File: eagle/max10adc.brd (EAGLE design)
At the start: 98 x 62 mm, 189 parts, among them IC1 MAX19506, IC2 MAX19506, J1 MOLEX_BNC_73100-0105, J2 MOLEX_BNC_73100-0105, J3 MOLEX_BNC_73100-0105, J4 MOLEX_BNC_73100-0105, K1 AQY21SOP, K2 AQY21SOP, K3 AQY21SOP, K4 AQY21SOP, K5 AQY21SOP, K6 AQY21SOP, K7 AQY21SOP, K8 AQY21SOP, U1 MAX4416ESA, U2 MAX4416ESA, U340G CH340G, Y1 ABL-12.000MHZ-B2

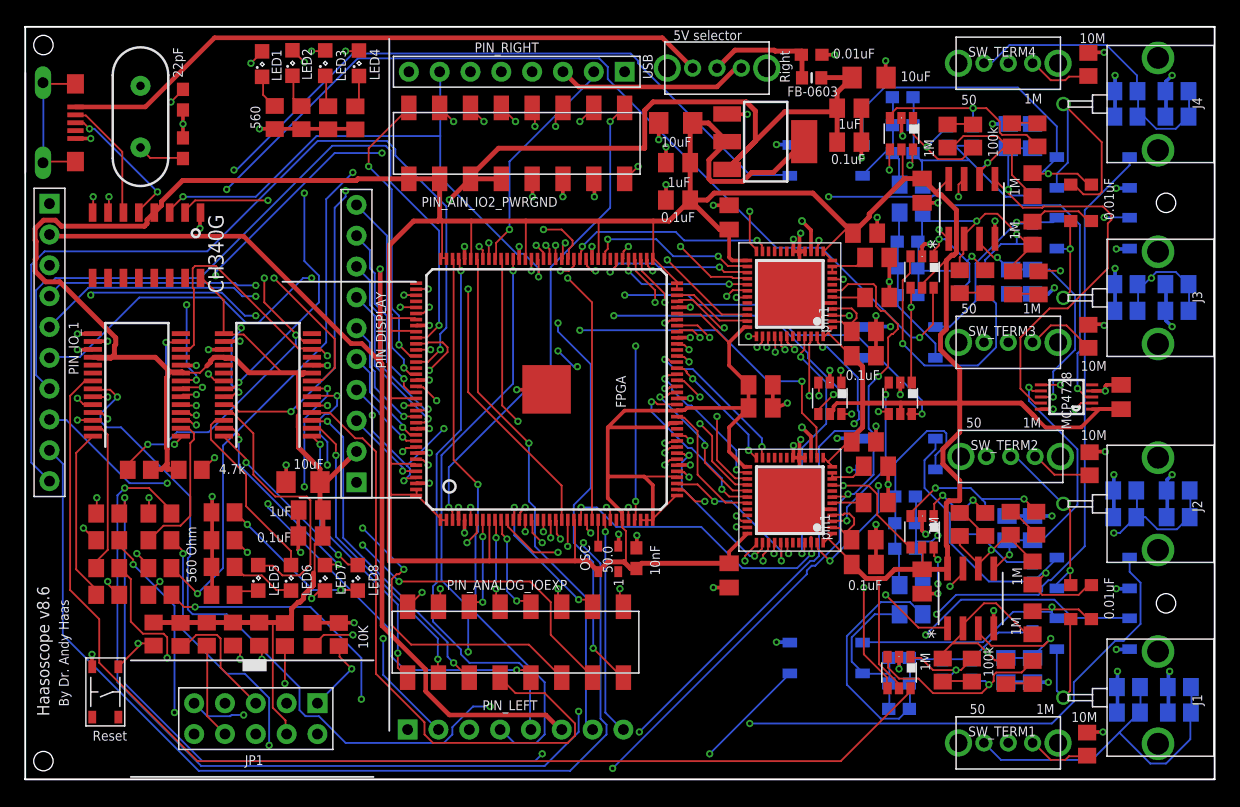
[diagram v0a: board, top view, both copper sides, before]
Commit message: for 8.7 with separate VCCA
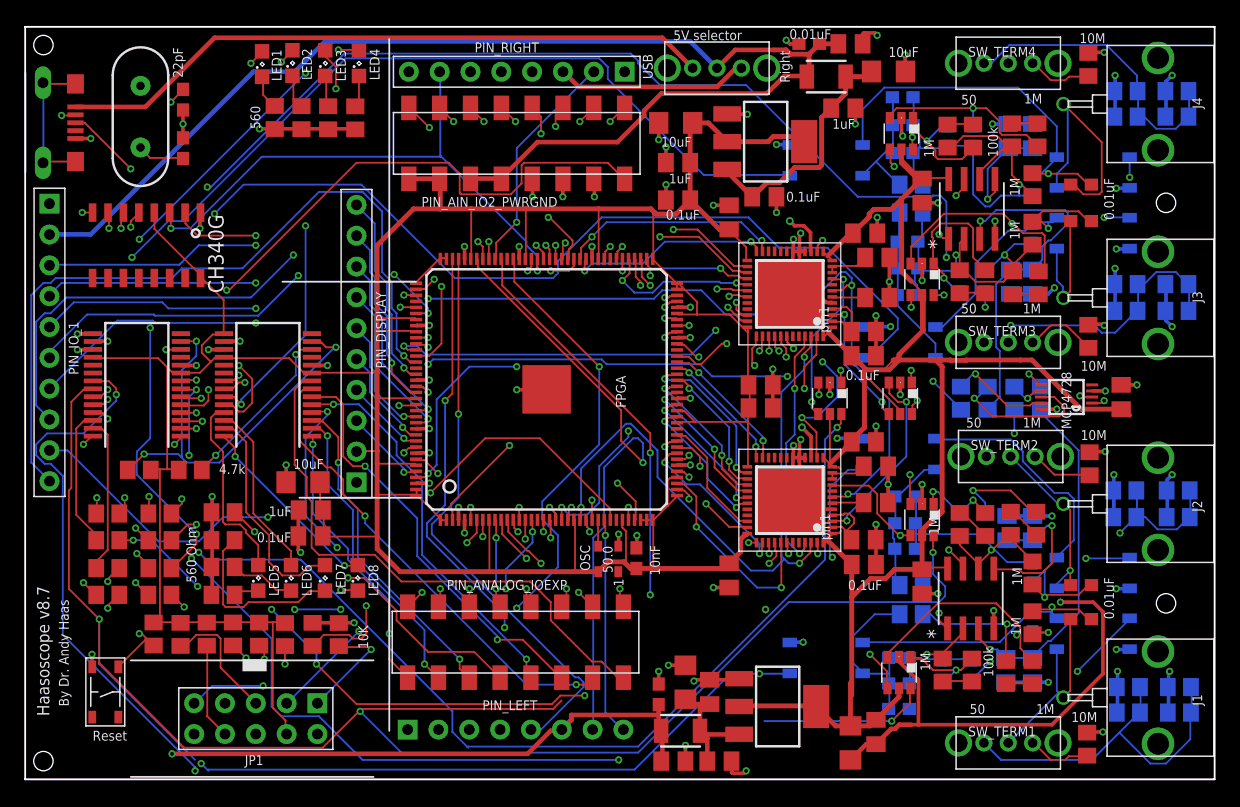
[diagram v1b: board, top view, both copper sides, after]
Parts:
- removed 5VBEAD: FB-0603, rcl:L0603
- added CP10, CP11, CP7, CP9: 1uF, rcl:C0805K
- added CP3, CP4: 10uF, rcl@1:C1206
- added CP8: 0.1uF, rcl:C0805K
- added C_5V_10NF1: 0.01uF, rcl@1:C0603
- added L1, L2: 10uH, SparkFun-Passives:1210
- added REG1: LDL1117S33R, Seeed-IC-2016:SOT-223
- added ROFFSET1, ROFFSET2, ROFFSET3, ROFFSET4: 200, rcl@1:R0805
- COFFSETB11, COFFSETB5, COFFSETB7, COFFSETB9: value 1uF -> 10uF
- moved CP2 8.32 mm to (48.9, 46.0)
- moved CP5 1.68 mm to (59.1, 56.3)
- moved GAINSW2 1.00 mm to (61.9, 19.4)
- moved C_5V_10NF 0.92 mm to (52.6, 58.6)
- moved GAINSW3 0.60 mm to (61.9, 39.2)
- moved CP1 0.50 mm to (55.4, 53.3)
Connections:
- removed net 5V_IN: 5VBEAD.2, C_5V_10NF.1, SW_5V.2
- new net N$44: DAC1.6, ROFFSET1.2
- new net N$45: DAC1.7, ROFFSET2.2
- new net N$46: DAC1.8, ROFFSET3.2
- new net N$47: DAC1.9, ROFFSET4.2
- new net N$48: CP3.1, CP7.1, CP8.1, L2.2, REG1.3
- new net N$49: CP1.1, CP2.1, CP5.1, L1.2, REG.3
- new net VCCA: C5VOPAMP1.1, C5VOPAMP2.1, CADD1_A.1, CADD1_B.1, CADD2_A.1, CADD2_B.1, COFFSET.2, CP4.1, CP9.1, DAC1.1, GAINSW1.5, GAINSW2.5, GAINSW3.5, GAINSW4.5, IC1.1, IC1.12, IC1.13, IC1.48, IC2.1, IC2.12, IC2.13, IC2.48, OVSAMP1.5, OVSAMP2.5, REG1.2, REG1.TER, U1.8, U2.8
- net +3V3: no longer C5VOPAMP1.1, C5VOPAMP2.1, CADD1_A.1, CADD1_B.1, CADD2_A.1, CADD2_B.1, COFFSET.2, DAC1.1, GAINSW1.5, GAINSW2.5, GAINSW3.5, GAINSW4.5, IC1.1, IC1.12, IC1.13, IC1.48, IC2.1, IC2.12, IC2.13, IC2.48, OVSAMP1.5, OVSAMP2.5, U1.8, U2.8
- net +5V: now also CP10.2, CP11.2, C_5V_10NF.2, C_5V_10NF1.2, L1.1, L2.1, SW_5V.2; no longer 5VBEAD.1, CP1.1, CP2.1, CP5.1, REG.3
- net GND: now also CP10.1, CP11.1, CP3.2, CP4.2, CP7.2, CP8.2, CP9.2, C_5V_10NF.1, C_5V_10NF1.1, REG1.1; no longer C_5V_10NF.2
- net OFFSET1: now also ROFFSET1.1; no longer DAC1.6
- net OFFSET2: now also ROFFSET2.1; no longer DAC1.7
- net OFFSET3: now also ROFFSET3.1; no longer DAC1.8
- net OFFSET4: now also ROFFSET4.1; no longer DAC1.9
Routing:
- net +3V3: track 554.7 -> 311.9 mm
- net VCCA: track 0.00 -> 209.3 mm
- net GND: track 199.0 -> 254.9 mm, vias 92 -> 100
- net +5V: track 148.2 -> 200.5 mm, vias 2 -> 1
- net E_GSW2: track 100.7 -> 142.8 mm, vias 4 -> 3
- net E_SHDN: track 127.0 -> 86.3 mm
- net L21_SDA: track 154.7 -> 114.1 mm, vias 7 -> 6
- net L141_SCL: track 117.4 -> 150.9 mm, vias 8 -> 6
- net E_OVSAMP2: track 61.1 -> 93.6 mm
- net IO_29: track 87.8 -> 60.9 mm
- net N$36: track 105.9 -> 79.3 mm, vias 3 -> 7
- net E_24_B7: track 71.2 -> 46.3 mm, vias 3 -> 0
- net IO_118: track 61.2 -> 40.2 mm, vias 1 -> 2
- net N$49: track 0.00 -> 20.4 mm
- net E_24_B3: track 53.2 -> 33.7 mm, vias 0 -> 3
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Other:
- board text added: "Haasoscope v8.7"
- board text removed: "Haasoscope v8.6"

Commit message: for 8.7 and USB2
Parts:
- moved LED4 49.6 mm to (0.00, 9.90)
- moved LED3 49.4 mm to (-2.18, 9.91)
- moved LED2 49.3 mm to (-4.38, 9.92)
- moved LED1 49.1 mm to (-6.58, 9.93)
- moved RLED1 39.3 mm to (8.53, 13.2), turned to 180 degrees
- moved RLED2 37.0 mm to (8.52, 15.5), turned to 180 degrees
- moved RLED3 35.1 mm to (8.51, 17.7), turned to 180 degrees
- moved RLED4 33.2 mm to (8.50, 20.0), turned to 180 degrees
- moved PIN_IO_1 25.6 mm to (15.4, 36.9), turned to 180 degrees
- moved PIN_DISPLAY 25.5 mm to (-10.0, 36.9), turned to 0 degrees
- moved RS9 17.7 mm to (15.4, 15.4), turned to 180 degrees
- moved USB1 15.8 mm to (4.10, 58.4), turned to 180 degrees
- moved RJ3 14.9 mm to (15.3, 13.3), turned to 180 degrees
- moved SW_RESET 13.6 mm to (-9.40, 18.2)
- moved RJ5 12.5 mm to (15.4, 11.1), turned to 180 degrees
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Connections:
- net +3V3: no longer PIN_DISPLAY.2
- net +5V: now also PIN_DISPLAY.2
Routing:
- net VCCA: track 209.3 -> 137.8 mm
- net +3V3: track 311.9 -> 379.7 mm, vias 0 -> 4
- net L141_SCL: track 150.9 -> 91.1 mm, vias 6 -> 8
- net E_OVSAMP1: track 64.8 -> 113.2 mm
- net L135: track 6.71 -> 52.1 mm, vias 1 -> 3
- net L140: track 6.95 -> 50.1 mm, vias 1 -> 4
- net IO_122: track 62.9 -> 20.4 mm
- net GND: track 254.9 -> 293.5 mm
- net IO_119: track 51.4 -> 13.5 mm, vias 2 -> 1
- net +5V: track 200.5 -> 166.0 mm, vias 1 -> 2
- net L134: track 8.57 -> 41.8 mm
- net L131: track 10.1 -> 41.9 mm, vias 1 -> 3
- net IO_118: track 40.2 -> 9.51 mm, vias 2 -> 1
- net E_GSW2: track 142.8 -> 112.7 mm
- net IO_114: track 37.1 -> 7.57 mm, vias 3 -> 1
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
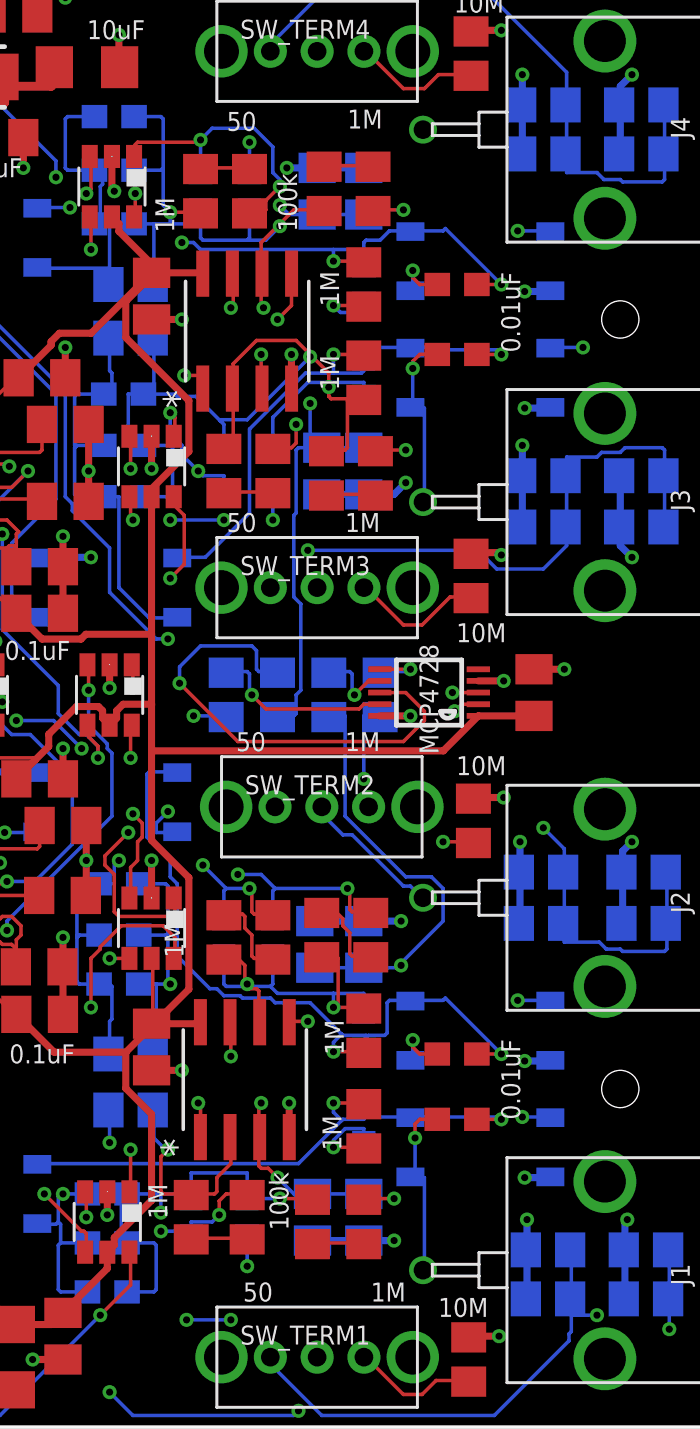
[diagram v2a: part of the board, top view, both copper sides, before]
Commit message: for 8.7 use 1210 10uF caps for offset
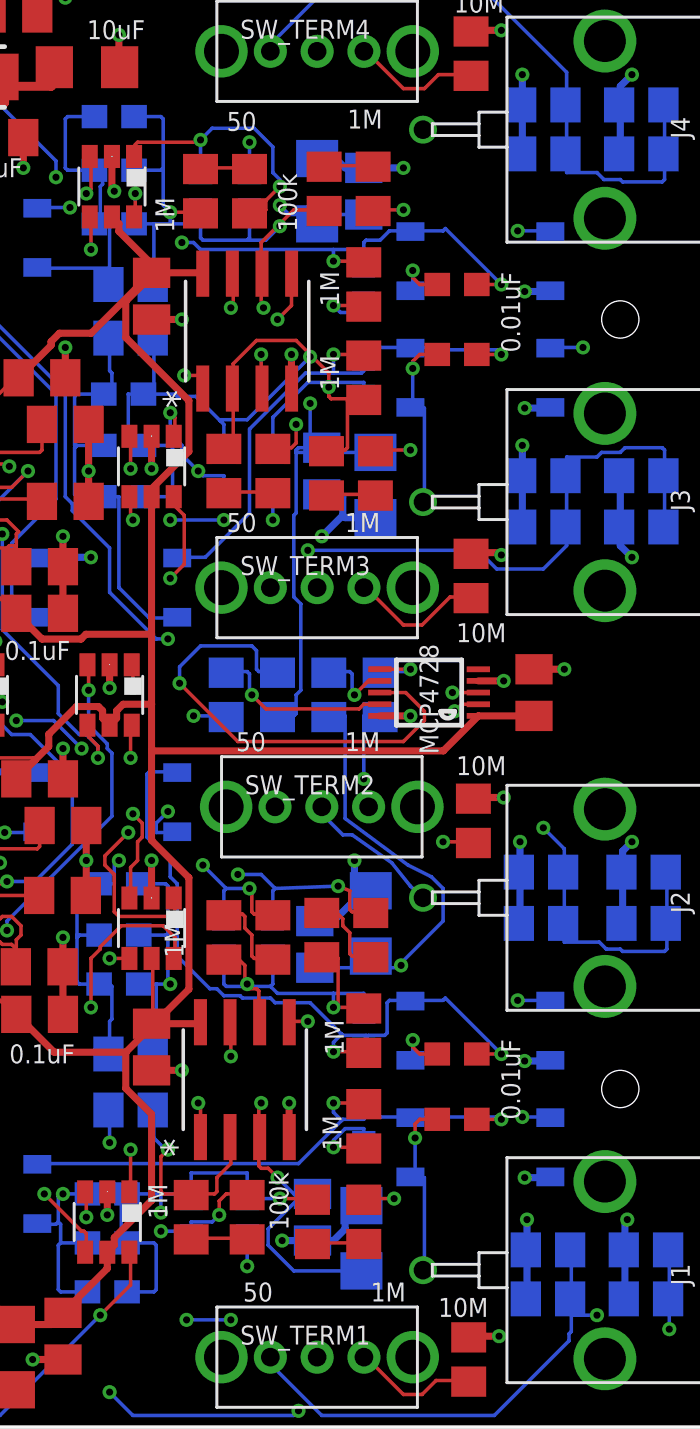
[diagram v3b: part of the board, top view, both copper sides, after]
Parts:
- removed COFFSETB11, COFFSETB5, COFFSETB7, COFFSETB9: 10uF, rcl:C0805K
- added COFFSETA1, COFFSETA2, COFFSETA3, COFFSETA6: 10uF, rcl@1:C1206
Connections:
- net GND: now also COFFSETA1.1, COFFSETA2.1, COFFSETA3.1, COFFSETA6.1; no longer COFFSETB11.1, COFFSETB5.1, COFFSETB7.1, COFFSETB9.1
- net OFFSET1: now also COFFSETA6.2; no longer COFFSETB5.2
- net OFFSET2: now also COFFSETA1.2; no longer COFFSETB7.2
- net OFFSET3: now also COFFSETA2.2; no longer COFFSETB9.2
- net OFFSET4: now also COFFSETA3.2; no longer COFFSETB11.2
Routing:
- net OFFSET1: track 26.9 -> 32.0 mm
- net GND: track 293.5 -> 297.1 mm
- net OFFSET3: track 21.7 -> 23.3 mm
- net OFFSET2: track 24.1 -> 24.7 mm

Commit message: for 8.7 fix some text etc
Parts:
- moved COFFSETA3 2.24 mm to (71.0, 52.0)
- moved COFFSETB12 2.18 mm to (68.9, 51.6)

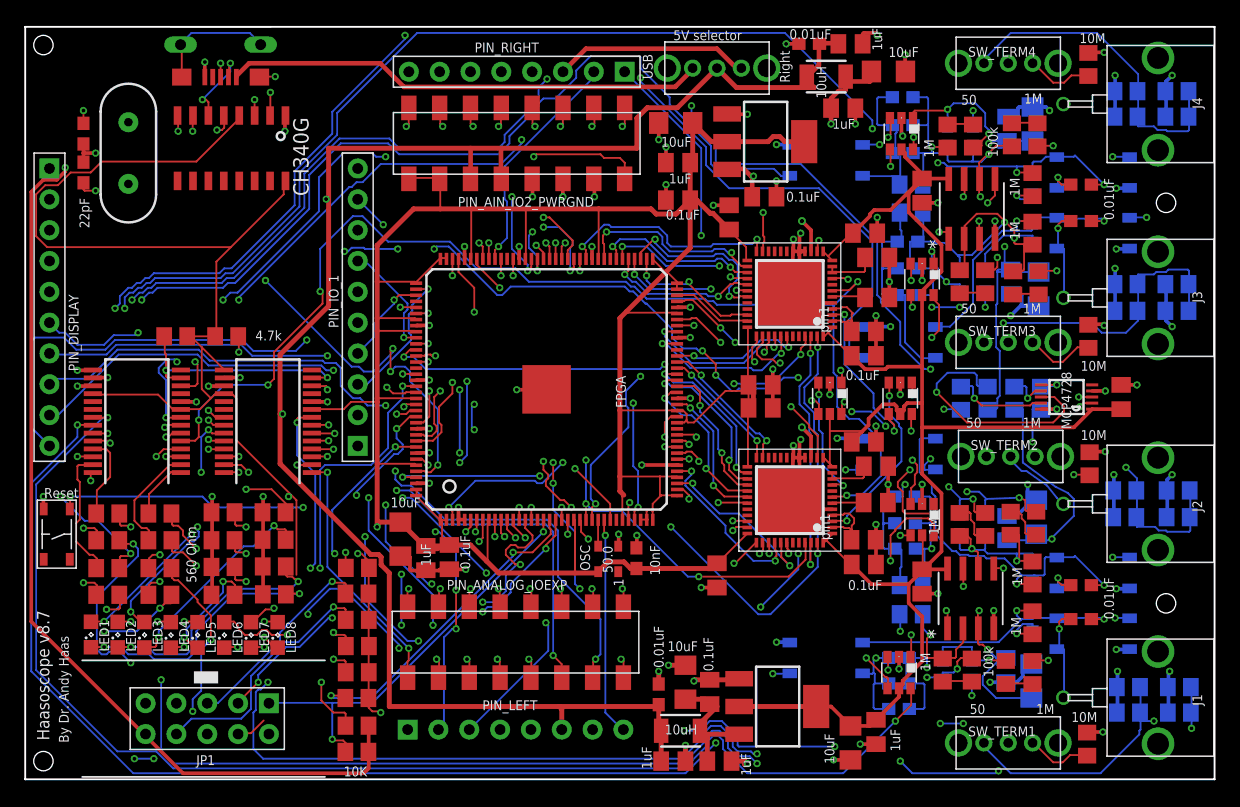
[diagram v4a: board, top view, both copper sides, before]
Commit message: v8.7 just ordered from AllPCB
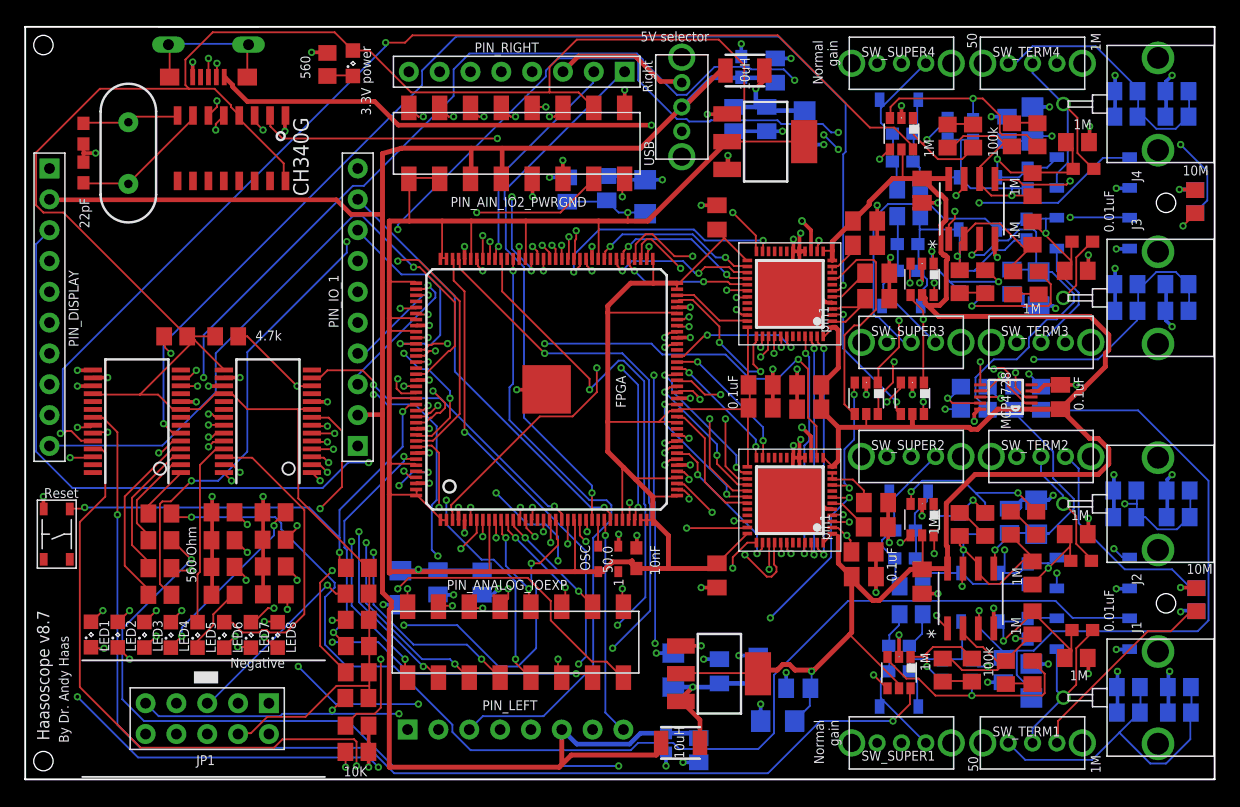
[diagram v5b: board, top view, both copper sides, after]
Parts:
- removed CIN1, CIN2, CIN3, CIN4: 10pF, rcl@1:C0603
- removed CIN56_5, CIN56_6, CIN56_7, CIN56_8: 56pF, rcl@1:C0603
- removed HGR1, HGR2, HGR3, HGR4: 560, resistor:R0805
- removed K5, K6, K7, K8: AQY21SOP, relay:SOP04
- added C1, C2, C3, C4: 3-10pF, SparkFun-Passives:CTZ3
- added CIN5_1, CIN5_2, CIN5_3, CIN5_4: 5pF, rcl@1:C0603
- added C_S1, C_S2, C_S3, C_S4: 8-45pF, SparkFun-Passives:CTZ3
- added LEDPOW: MF-LED-0805-RED, led:SML0805
- added RIN5, RIN6, RIN7, RIN8: 1M, resistor:R0805
- added RLEDPOW: 560, resistor:R0805
- added SW_SUPER1, SW_SUPER2, SW_SUPER3, SW_SUPER4: 0S102011MS2QS1, PP_Electromechanical:0S102011MS2QS1
- moved CIN56_4 29.9 mm to (60.3, 51.2)
- moved CIN56_3 20.8 mm to (60.7, 39.9)
- moved R10M_1 14.9 mm to (84.5, 12.8)
- moved CIN56_2 14.7 mm to (60.5, 18.5)
- moved R10M_4 14.3 mm to (84.4, 45.6), flipped to the bottom
- moved R10M_2 14.2 mm to (84.5, 12.8), flipped to the bottom, turned to 90 degrees
- moved R10M_3 14.2 mm to (84.4, 45.6)
- moved CV11 9.16 mm to (32.7, 46.6), flipped to the bottom, turned to 90 degrees
- moved CP5 8.33 mm to (52.2, 51.7), flipped to the bottom, turned to 270 degrees
- moved CP7 7.40 mm to (45.2, 6.90), flipped to the bottom, turned to 90 degrees
- moved CP9 7.34 mm to (51.7, 5.50), flipped to the bottom, turned to 0 degrees
- moved CP2 6.87 mm to (46.4, 52.4), flipped to the bottom, turned to 270 degrees
- moved L1 6.72 mm to (47.3, 56.4)
- moved CP6 6.58 mm to (39.1, 46.0), flipped to the bottom, turned to 90 degrees
- moved CP11 6.58 mm to (49.8, 56.4), flipped to the bottom, turned to 270 degrees
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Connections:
- removed net E_20_B7: IOEXPAND_0X20_BOT.8, PIN_AIN_IO2_PWRGND.2
- removed net E_HIGHGAIN1: HGR1.1, IOEXPAND_0X20_BOT.25
- removed net E_HIGHGAIN2: HGR2.1, IOEXPAND_0X20_BOT.26
- removed net E_HIGHGAIN3: HGR3.1, IOEXPAND_0X20_BOT.27
- removed net E_HIGHGAIN4: HGR4.1, IOEXPAND_0X20_BOT.28
- removed net E_SHDN: IC1.7, IC2.7, IOEXPAND_0X20_BOT.5
- removed net N$36: HGR2.2, K6.1
- removed net N$37: HGR3.2, K7.1
- removed net N$43: HGR4.2, K8.1
- new net E_SHDN1: IC1.7, IOEXPAND_0X20_BOT.5
- new net E_SHDN2: IC2.7, IOEXPAND_0X20_BOT.6
- net +3V3: now also LEDPOW.A, PIN_AIN_IO2_PWRGND.3
- net AIN1: now also PIN_AIN_IO2_PWRGND.2; no longer PIN_AIN_IO2_PWRGND.1
- net E_OVSAMP1: now also IOEXPAND_0X20_BOT.25; no longer IOEXPAND_0X20_BOT.6
- net E_OVSAMP2: now also IOEXPAND_0X20_BOT.26; no longer IOEXPAND_0X20_BOT.7
- net GND: now also PIN_AIN_IO2_PWRGND.1, RIN5.2, RIN6.2, RIN7.2, RIN8.2, RLEDPOW.2; no longer K5.2, K6.2, K7.2, K8.2, PIN_AIN_IO2_PWRGND.4
- net INAMINUS1: now also C1.-, CIN5_1.1, C_S1.-; no longer CIN1.2, CIN56_2.2
- net INAMINUS2: now also C3.-, CIN56_3.2, CIN5_3.1, C_S3.-; no longer CIN3.2, CIN56_5.2, CIN56_6.2
- net INBMINUS1: now also C2.-, CIN56_2.2, CIN5_2.1, C_S2.-; no longer CIN2.2, CIN56_3.2, CIN56_4.2
- net INBMINUS2: now also C4.-, CIN56_4.2, CIN5_4.1, C_S4.-; no longer CIN4.2, CIN56_7.2, CIN56_8.2
- net IO_100: now also PIN_AIN_IO2_PWRGND.13; no longer PIN_AIN_IO2_PWRGND.11
- net IO_101: now also PIN_AIN_IO2_PWRGND.15; no longer PIN_AIN_IO2_PWRGND.13
- net IO_CLK_88: now also PIN_AIN_IO2_PWRGND.5; no longer PIN_AIN_IO2_PWRGND.3
- net IO_CLK_89: now also PIN_AIN_IO2_PWRGND.7; no longer PIN_AIN_IO2_PWRGND.5
- net IO_CLK_90: now also PIN_AIN_IO2_PWRGND.9; no longer PIN_AIN_IO2_PWRGND.7
- net IO_CLK_91: now also PIN_AIN_IO2_PWRGND.11; no longer PIN_AIN_IO2_PWRGND.9
- net L121: now also PIN_AIN_IO2_PWRGND.4; no longer PIN_AIN_IO2_PWRGND.15
- net N$10: now also C1.+, CIN5_1.2, RIN5.1, SW_SUPER1.2; no longer CIN1.1, K5.3
- net N$15: now also C2.+, CIN5_2.2, RIN6.1, SW_SUPER2.2; no longer CIN2.1, K6.3
- net N$20: now also C_S1.+, SW_SUPER1.3; no longer CIN56_2.1, K5.4
- net N$34: now also LEDPOW.C, RLEDPOW.1; no longer HGR1.2, K5.1
- net N$38: now also CIN56_2.1, C_S2.+, SW_SUPER2.3; no longer CIN56_3.1, CIN56_4.1, K6.4
- net N$39: now also C3.+, CIN5_3.2, RIN7.1, SW_SUPER3.2; no longer CIN3.1, K7.3
- net N$40: now also CIN56_3.1, C_S3.+, SW_SUPER3.3; no longer CIN56_5.1, CIN56_6.1, K7.4
- net N$41: now also C4.+, CIN5_4.2, RIN8.1, SW_SUPER4.2; no longer CIN4.1, K8.3
- net N$42: now also CIN56_4.1, C_S4.+, SW_SUPER4.3; no longer CIN56_7.1, CIN56_8.1, K8.4
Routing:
- net N$37: track 135.7 -> 0.00 mm, vias 3 -> 0
- net N$43: track 100.3 -> 0.00 mm, vias 2 -> 0
- net N$36: track 99.1 -> 0.00 mm, vias 5 -> 0
- net E_SHDN: track 96.1 -> 0.00 mm, vias 5 -> 0
- net E_SHDN1: track 0.00 -> 95.1 mm, vias 0 -> 5
- net E_SHDN2: track 0.00 -> 94.2 mm, vias 0 -> 2
- net N$34: track 79.1 -> 2.20 mm, vias 2 -> 0
- net GND: track 297.6 -> 222.5 mm, vias 100 -> 102
- net E_20_B7: track 54.7 -> 0.00 mm, vias 5 -> 0
- net +3V3: track 379.7 -> 426.9 mm, vias 4 -> 2
- net N$32: track 154.0 -> 118.8 mm, vias 7 -> 4
- net E_OVSAMP2: track 93.7 -> 126.6 mm, vias 8 -> 2
- net VCCA: track 137.8 -> 168.0 mm, vias 0 -> 1
- net OFFSET1: track 32.0 -> 56.7 mm, vias 3 -> 1
- net N$35: track 140.0 -> 116.4 mm
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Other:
- board text added: "1nF+56pF"
- board text added: "200"
- board text added: "3.3V power"
- board text added: "560"
- board text added: "5pF"
- board text added: "Negative"
- board text added: "Normal gain"
- board text added: "Super-gain"
- board text removed: "1nF+56pFx2"
- board text removed: "1uF"
- board text removed: "200 Ohm (x4)"
